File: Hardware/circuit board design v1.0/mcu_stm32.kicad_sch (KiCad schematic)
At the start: 1 part, among them U1 STM32F303RCTx

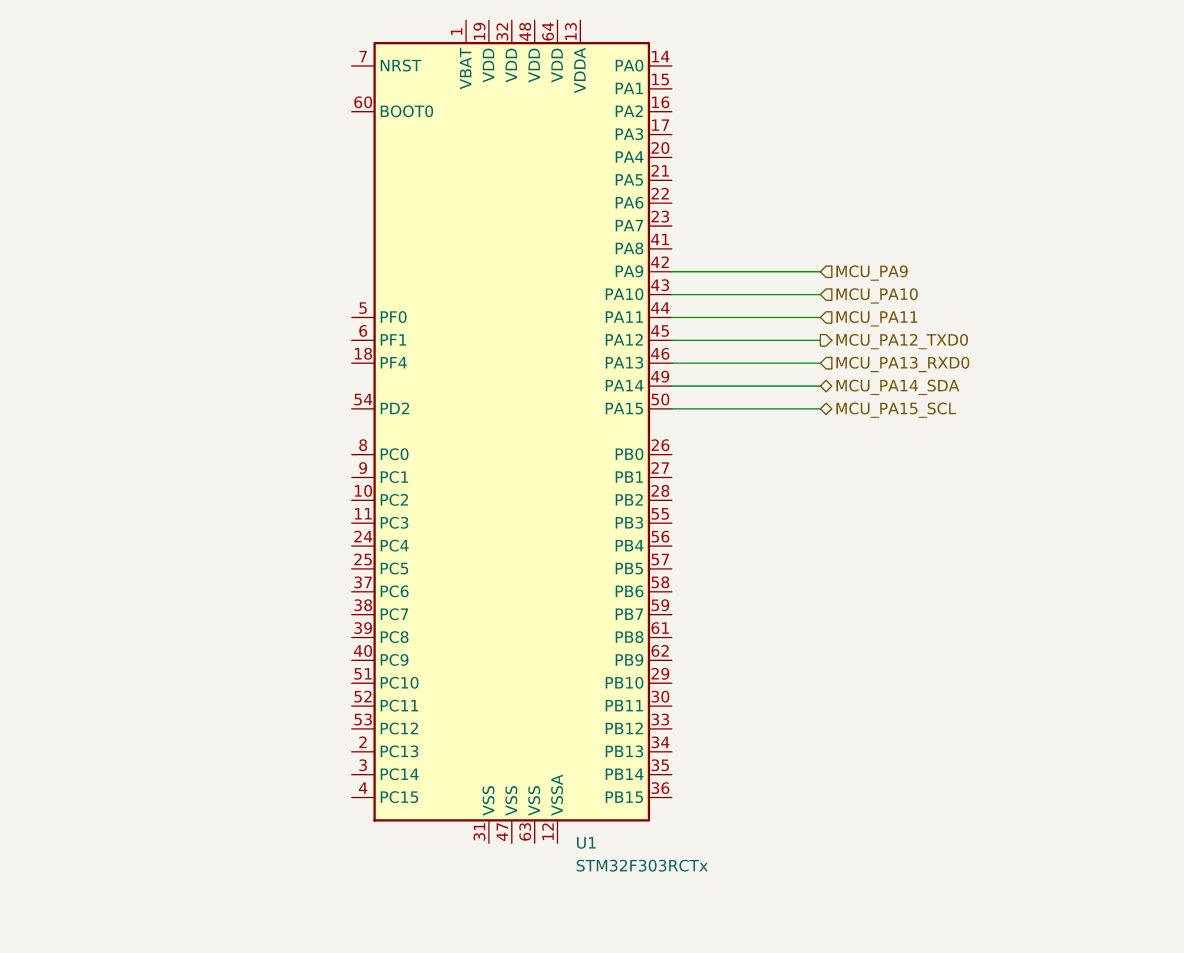
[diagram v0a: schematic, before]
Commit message: Added new diagram and symbol library
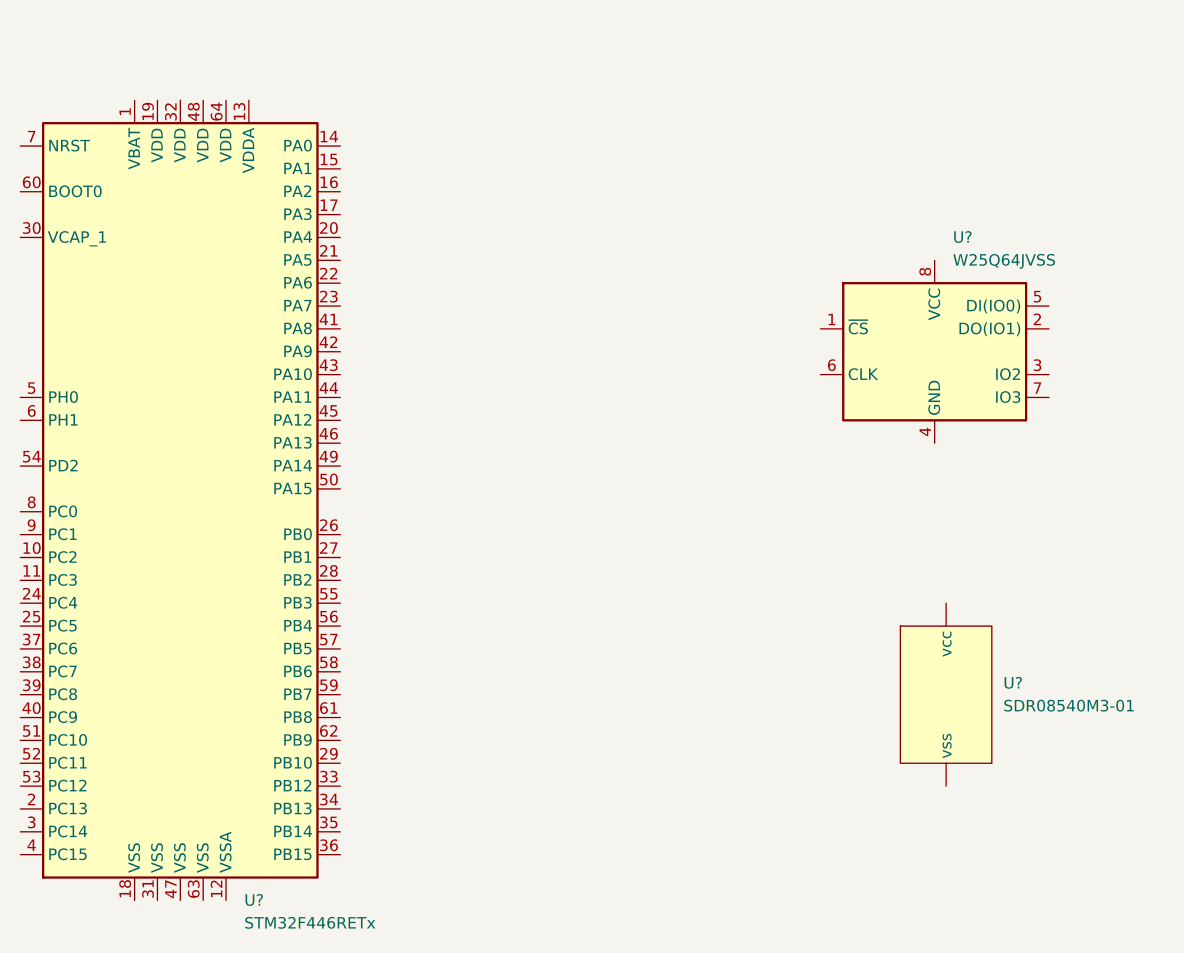
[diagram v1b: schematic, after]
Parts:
- removed U1: STM32F303RCTx, Package_QFP:LQFP-64_10x10mm_P0.5mm, symbol MCU_ST_STM32F3:STM32F303RCTx
- added U?: SDR08540M3-01, symbol Components:SDR08540M3-01
- added U?: W25Q64JVSS, Package_SO:SOIC-8_5.23x5.23mm_P1.27mm, symbol Components:W25Q64JVSS
- added U?: STM32F446RETx, Package_QFP:LQFP-64_10x10mm_P0.5mm, symbol MCU_ST_STM32F4:STM32F446RETx
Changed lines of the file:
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@@
 (kicad_sch (version 20211123) (generator eeschema)
   (paper "A4")
-  (wire (pts (xy 204.47 83.82) (xy 220.98 83.82))
-    (stroke (width 0) (type default) (color 0 0 0 0))
-  )
-  (wire (pts (xy 204.47 76.2) (xy 220.98 76.2))
-    (stroke (width 0) (type default) (color 0 0 0 0))
-  )
-  (wire (pts (xy 204.47 68.58) (xy 220.98 68.58))
-    (stroke (width 0) (type default) (color 0 0 0 0))
-  )
-  (wire (pts (xy 204.47 81.28) (xy 220.98 81.28))
-    (stroke (width 0) (type default) (color 0 0 0 0))
-  )
-  (wire (pts (xy 204.47 71.12) (xy 220.98 71.12))
-    (stroke (width 0) (type default) (color 0 0 0 0))
-  )
-  (wire (pts (xy 204.47 78.74) (xy 220.98 78.74))
-    (stroke (width 0) (type default) (color 0 0 0 0))
-  )
-  (wire (pts (xy 204.47 73.66) (xy 220.98 73.66))
-    (stroke (width 0) (type default) (color 0 0 0 0))
-  )
-  (hierarchical_label "MCU_PA15_SCL" (shape bidirectional) (at 220.98 83.82 0)
-    (effects (font (size 1.27 1.27)) (justify left))
-  )
-  (hierarchical_label "MCU_PA11" (shape input) (at 220.98 73.66 0)
-    (effects (font (size 1.27 1.27)) (justify left))
-  )
-  (hierarchical_label "MCU_PA12_TXD0" (shape output) (at 220.98 76.2 0)
-    (effects (font (size 1.27 1.27)) (justify left))
-  )
-  (hierarchical_label "MCU_PA9" (shape input) (at 220.98 68.58 0)
-    (effects (font (size 1.27 1.27)) (justify left))
-  )
-  (hierarchical_label "MCU_PA13_RXD0" (shape input) (at 220.98 78.74 0)
-    (effects (font (size 1.27 1.27)) (justify left))
-  )
-  (hierarchical_label "MCU_PA14_SDA" (shape bidirectional) (at 220.98 81.28 0)
-    (effects (font (size 1.27 1.27)) (justify left))
-  )
-  (hierarchical_label "MCU_PA10" (shape input) (at 220.98 71.12 0)
-    (effects (font (size 1.27 1.27)) (justify left))
-  )
-  (symbol (lib_id "MCU_ST_STM32F3:STM32F303RCTx") (at 186.69 86.36 0) (unit 1)
+  (symbol (lib_name "SDR08540M3-01_1") (lib_id "Components:SDR08540M3-01") (at 234.95 116.84 0) (unit 1)
     (in_bom yes) (on_board yes) (fields_autoplaced)
-    (property "Reference" "U1" (id 0) (at 193.7894 132.08 0)
+    (property "Reference" "U?" (id 0) (at 241.3 114.2999 0)
       (effects (font (size 1.27 1.27)) (justify left))
     )
-    (property "Value" "STM32F303RCTx" (id 1) (at 193.7894 134.62 0)
+    (property "Value" "SDR08540M3-01" (id 1) (at 241.3 116.8399 0)
       (effects (font (size 1.27 1.27)) (justify left))
     )
-    (property "Footprint" "Package_QFP:LQFP-64_10x10mm_P0.5mm" (id 2) (at 171.45 129.54 0)
+    (property "Footprint" "" (id 2) (at 234.95 116.84 0)
+      (effects (font (size 1.27 1.27)) hide)
+    )
+    (property "Datasheet" "https://docs.rs-online.com/16ce/0900766b815934ae.pdf" (id 3) (at 234.95 116.84 0)
+      (effects (font (size 1.27 1.27)) hide)
+    )
+    (pin "")
+    (pin "")
+  )
+  (symbol (lib_id "Components:W25Q64JVSS") (at 233.68 77.47 0) (unit 1)
+    (in_bom yes) (on_board yes) (fields_autoplaced)
+    (property "Reference" "U?" (id 0) (at 235.6994 64.77 0)
+      (effects (font (size 1.27 1.27)) (justify left))
+    )
+    (property "Value" "W25Q64JVSS" (id 1) (at 235.6994 67.31 0)
+      (effects (font (size 1.27 1.27)) (justify left))
+    )
+    (property "Footprint" "Package_SO:SOIC-8_5.23x5.23mm_P1.27mm" (id 2) (at 233.68 77.47 0)
+      (effects (font (size 1.27 1.27)) hide)
+    )
+    (property "Datasheet" "https://www.winbond.com/resource-files/W25Q64JV%20RevK%2003102021%20Plus.pdf#toolbar=0" (id 3) (at 233.68 77.47 0)
+      (effects (font (size 1.27 1.27)) hide)
+    )
+    (pin "1")
+    (pin "2")
+    (pin "3")
+    (pin "4")
+    (pin "5")
+    (pin "6")
+    (pin "7")
+    (pin "8")
+  )
+  (symbol (lib_id "MCU_ST_STM32F4:STM32F446RETx") (at 149.86 92.71 0) (unit 1)
+    (in_bom yes) (on_board yes) (fields_autoplaced)
+    (property "Reference" "U?" (id 0) (at 156.9594 138.43 0)
+      (effects (font (size 1.27 1.27)) (justify left))
+    )
+    (property "Value" "STM32F446RETx" (id 1) (at 156.9594 140.97 0)
+      (effects (font (size 1.27 1.27)) (justify left))
+    )
+    (property "Footprint" "Package_QFP:LQFP-64_10x10mm_P0.5mm" (id 2) (at 134.62 135.89 0)
       (effects (font (size 1.27 1.27)) (justify right) hide)
     )
-    (property "Datasheet" "http://www.st.com/st-web-ui/static/active/en/resource/technical/document/datasheet/DM00058181.pdf" (id 3) (at 186.69 86.36 0)
+    (property "Datasheet" "http://www.st.com/st-web-ui/static/active/en/resource/technical/document/datasheet/DM00141306.pdf" (id 3) (at 149.86 92.71 0)
       (effects (font (size 1.27 1.27)) hide)
     )

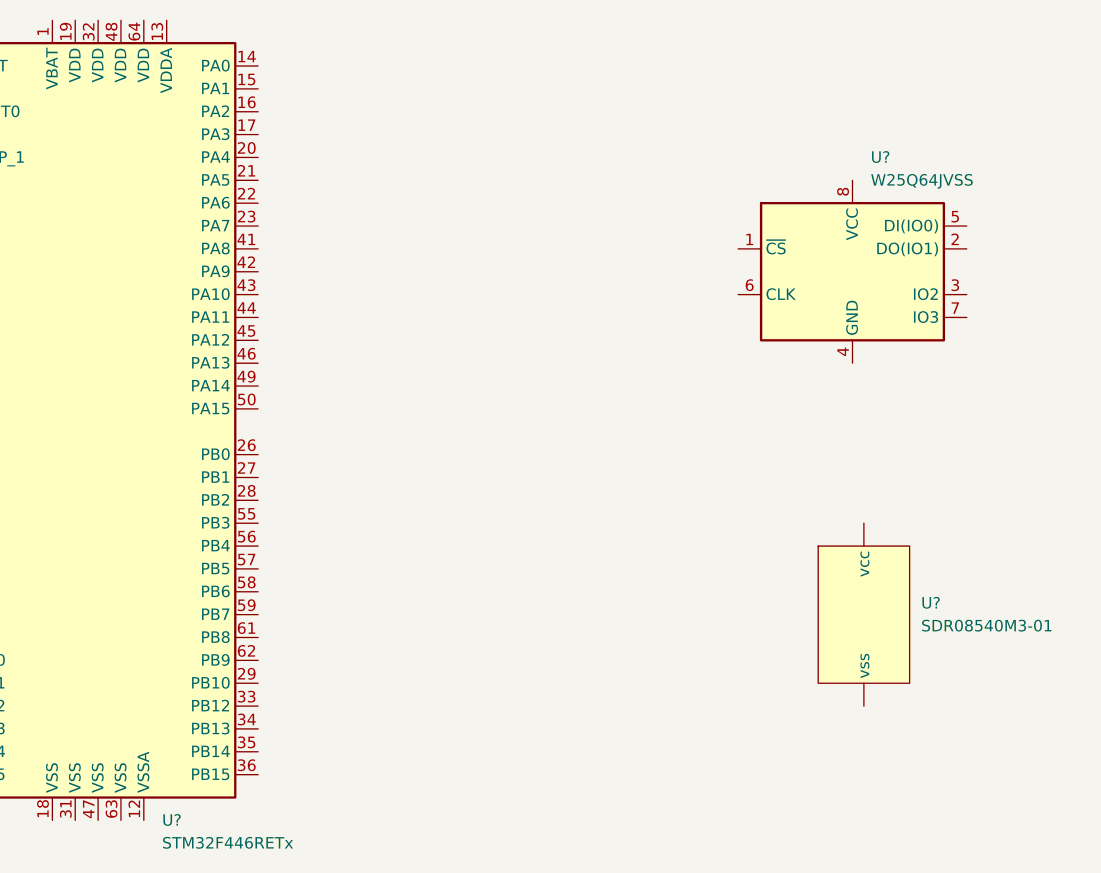
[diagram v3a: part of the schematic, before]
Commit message: BMI088 schematic
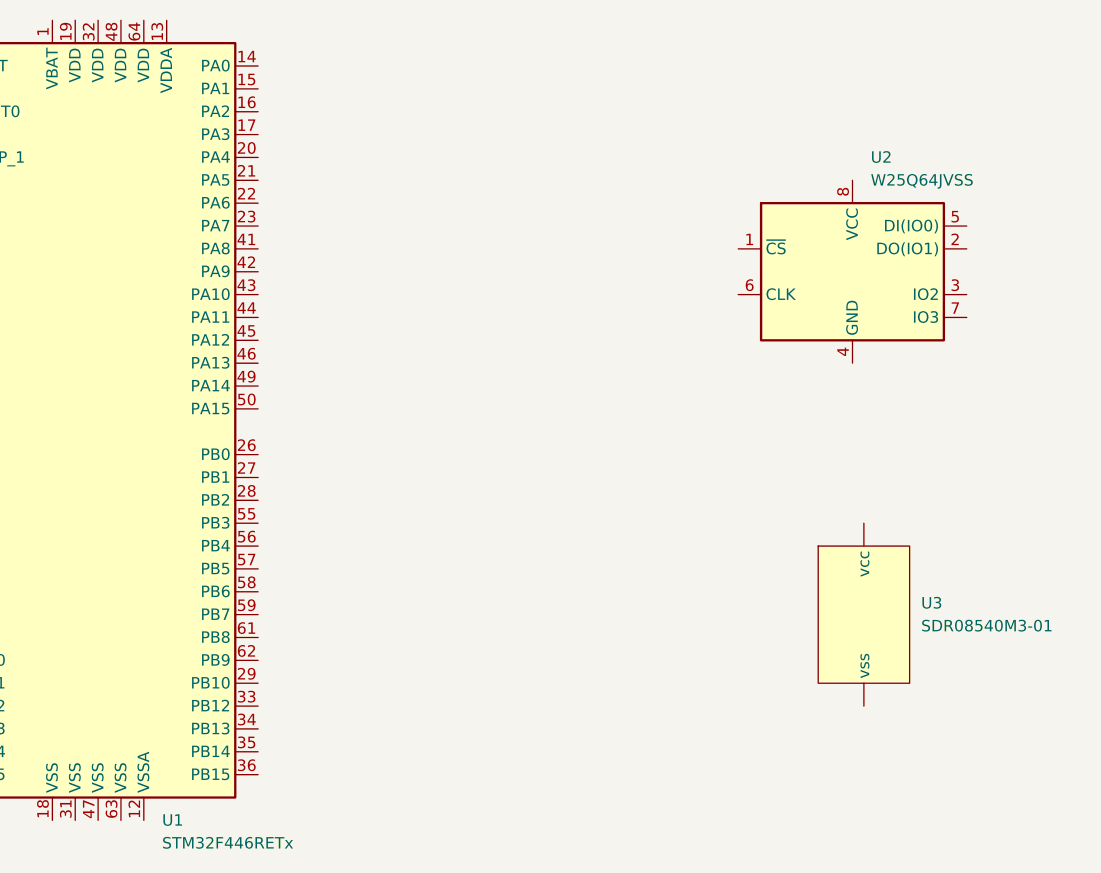
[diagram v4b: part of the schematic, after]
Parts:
- gave numbers to parts that had none: 3
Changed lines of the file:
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@@
   (symbol (lib_name "SDR08540M3-01_1") (lib_id "Components:SDR08540M3-01") (at 234.95 116.84 0) (unit 1)
     (in_bom yes) (on_board yes) (fields_autoplaced)
-    (property "Reference" "U?" (id 0) (at 241.3 114.2999 0)
+    (property "Reference" "U3" (id 0) (at 241.3 114.2999 0)
       (effects (font (size 1.27 1.27)) (justify left))
     )
@@
   (symbol (lib_id "Components:W25Q64JVSS") (at 233.68 77.47 0) (unit 1)
     (in_bom yes) (on_board yes) (fields_autoplaced)
-    (property "Reference" "U?" (id 0) (at 235.6994 64.77 0)
+    (property "Reference" "U2" (id 0) (at 235.6994 64.77 0)
       (effects (font (size 1.27 1.27)) (justify left))
     )
@@
   (symbol (lib_id "MCU_ST_STM32F4:STM32F446RETx") (at 149.86 92.71 0) (unit 1)
     (in_bom yes) (on_board yes) (fields_autoplaced)
-    (property "Reference" "U?" (id 0) (at 156.9594 138.43 0)
+    (property "Reference" "U1" (id 0) (at 156.9594 138.43 0)
       (effects (font (size 1.27 1.27)) (justify left))
     )

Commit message: Continued layout for PCB
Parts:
- added C? (x6): 100n, Capacitor_SMD:C_0603_1608Metric, symbol Device:C_Small
- added C?: 4.7u, Capacitor_THT:CP_Radial_D10.0mm_P5.00mm, symbol Device:C_Polarized_Small
- added D?: D_Schottky, symbol Device:D_Schottky
- added Q?: 2N7002-7-F, SOT96P240X120-3N, symbol Components:2N7002-7-F
- added R?: 68, Resistor_SMD:R_0603_1608Metric_Pad0.98x0.95mm_HandSolder, symbol Device:R
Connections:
- net GND: now reaches U3. (vss)
- net GND: now also U1.12 (VSSA), U1.18 (VSS), U1.31 (VSS), U1.47 (VSS), U1.63 (VSS), U2.4 (GND), C?.2, C?.2, C?.2, C?.2, C?.2, C?.2, C?.2, Q?.2
- net +3.3V: now reaches U2.8 (VCC)
- net +3.3V: now also U1.19 (VDD), U1.32 (VDD), U1.48 (VDD), U1.64 (VDD), U3. (vss), C?.1, C?.1, C?.1, C?.1, C?.1, D?.1 (K)
- net +3.3VA: now reaches U1.13 (VDDA)
- net +3.3VA: now also C?.1
- net at U1.30 (VCAP_1): now also C?.1
- net SCL: now reaches U1.58 (PB6)
- net SDA: now reaches U1.59 (PB7)
- new net: D?.2 (A), R?.1
- new net: Q?.3, R?.2
- no-connect marks 0 -> 51
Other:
- note added: "Might need additional filtering for analog vdd"
- moved on the sheet: U3

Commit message: Added buzzer transistor footprint
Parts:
- Q?: footprint SOT96P240X120-3N -> Components:SOT96P240X120-3N
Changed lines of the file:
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@@
       (effects (font (size 1.27 1.27)) (justify left))
     )
-    (property "Footprint" "SOT96P240X120-3N" (id 2) (at 240.03 146.05 0)
+    (property "Footprint" "Components:SOT96P240X120-3N" (id 2) (at 240.03 146.05 0)
       (effects (font (size 1.27 1.27)) (justify left) hide)
     )
